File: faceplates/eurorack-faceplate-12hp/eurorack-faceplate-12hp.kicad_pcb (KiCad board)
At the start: 2 copper layers, 60.6 x 133.3 mm, 4 parts

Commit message: Moving mounting holes
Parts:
- moved REF** 2.42 mm to (5.08, 130.3)
- moved REF** 2.42 mm to (5.08, 3.00)
- moved REF** 2.30 mm to (55.5, 130.3)
- moved REF** 2.30 mm to (55.5, 3.00)
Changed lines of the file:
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@@
   (net 0 "")
   (footprint "MountingHole:MountingHole_3.2mm_M3" (layer "F.Cu")
-    (at 7.5 130.35)
+    (at 5.08 130.35)
     (descr "Mounting Hole 3.2mm, no annular, M3")
     (tags "mounting hole 3.2mm no annular m3")
@@
   )
   (footprint "MountingHole:MountingHole_3.2mm_M3" (layer "F.Cu")
-    (at 53.22 130.35)
+    (at 55.52 130.35)
     (descr "Mounting Hole 3.2mm, no annular, M3")
     (tags "mounting hole 3.2mm no annular m3")
@@
   )
   (footprint "MountingHole:MountingHole_3.2mm_M3" (layer "F.Cu")
-    (at 53.22 3)
+    (at 55.52 3)
     (descr "Mounting Hole 3.2mm, no annular, M3")
     (tags "mounting hole 3.2mm no annular m3")
@@
   )
   (footprint "MountingHole:MountingHole_3.2mm_M3" (layer "F.Cu")
-    (at 7.5 3)
+    (at 5.08 3)
     (descr "Mounting Hole 3.2mm, no annular, M3")
     (tags "mounting hole 3.2mm no annular m3")

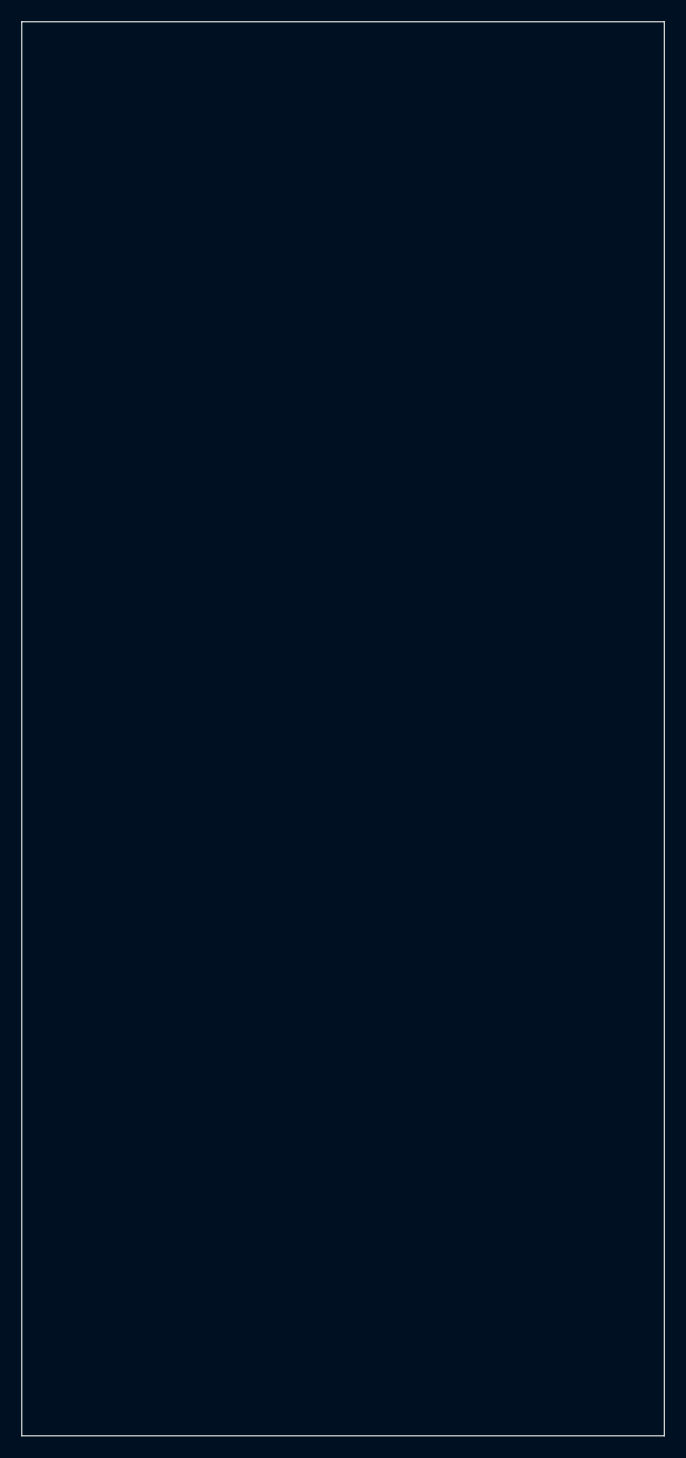
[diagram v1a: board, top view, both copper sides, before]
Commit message: Correcting panel height
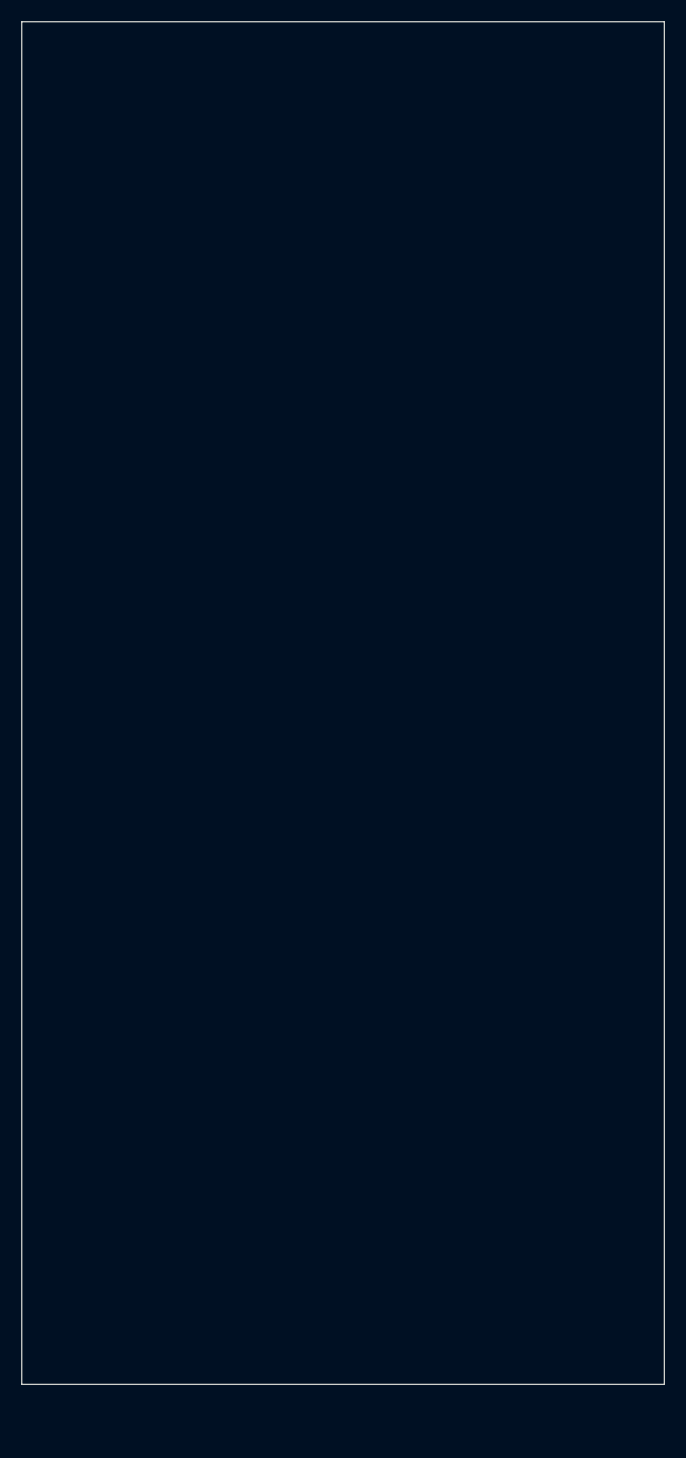
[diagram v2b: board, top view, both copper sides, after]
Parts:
- moved REF** 4.85 mm to (5.08, 125.5)
- moved REF** 4.85 mm to (55.5, 125.5)
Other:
- board size 60.6 x 133.3 mm -> 60.6 x 128.5 mm
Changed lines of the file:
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@@
   (net 0 "")
   (footprint "MountingHole:MountingHole_3.2mm_M3" (layer "F.Cu")
-    (at 5.08 130.35)
+    (at 5.08 125.5)
     (descr "Mounting Hole 3.2mm, no annular, M3")
     (tags "mounting hole 3.2mm no annular m3")
@@
   )
   (footprint "MountingHole:MountingHole_3.2mm_M3" (layer "F.Cu")
-    (at 55.52 130.35)
+    (at 55.52 125.5)
     (descr "Mounting Hole 3.2mm, no annular, M3")
     (tags "mounting hole 3.2mm no annular m3")
@@
     (pad "" np_thru_hole oval locked (at 0 0) (size 7 3.2) (drill oval 7 3.2) (layers F&B.Cu *.Mask))
   )
-  (gr_line (start 60.6 0) (end 60.6 133.35) (layer "Edge.Cuts") (width 0.1))
-  (gr_line (start 0 133.35) (end 0 0) (layer "Edge.Cuts") (width 0.1))
+  (gr_line (start 60.6 0) (end 60.6 128.5) (layer "Edge.Cuts") (width 0.1))
+  (gr_line (start 0 128.5) (end 0 0) (layer "Edge.Cuts") (width 0.1))
   (gr_line (start 0 0) (end 60.6 0) (layer "Edge.Cuts") (width 0.1))
-  (gr_line (start 60.6 133.35) (end 0 133.35) (layer "Edge.Cuts") (width 0.1))
+  (gr_line (start 60.6 128.5) (end 0 128.5) (layer "Edge.Cuts") (width 0.1))
 )
